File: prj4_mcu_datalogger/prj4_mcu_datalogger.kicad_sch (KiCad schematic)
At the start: 25 parts, among them U1 24LC1025, U2 24LC1025, U3 DS1337S+, U4 ATMEGA328P-AU, Y1 Crystal, Y2 Crystal

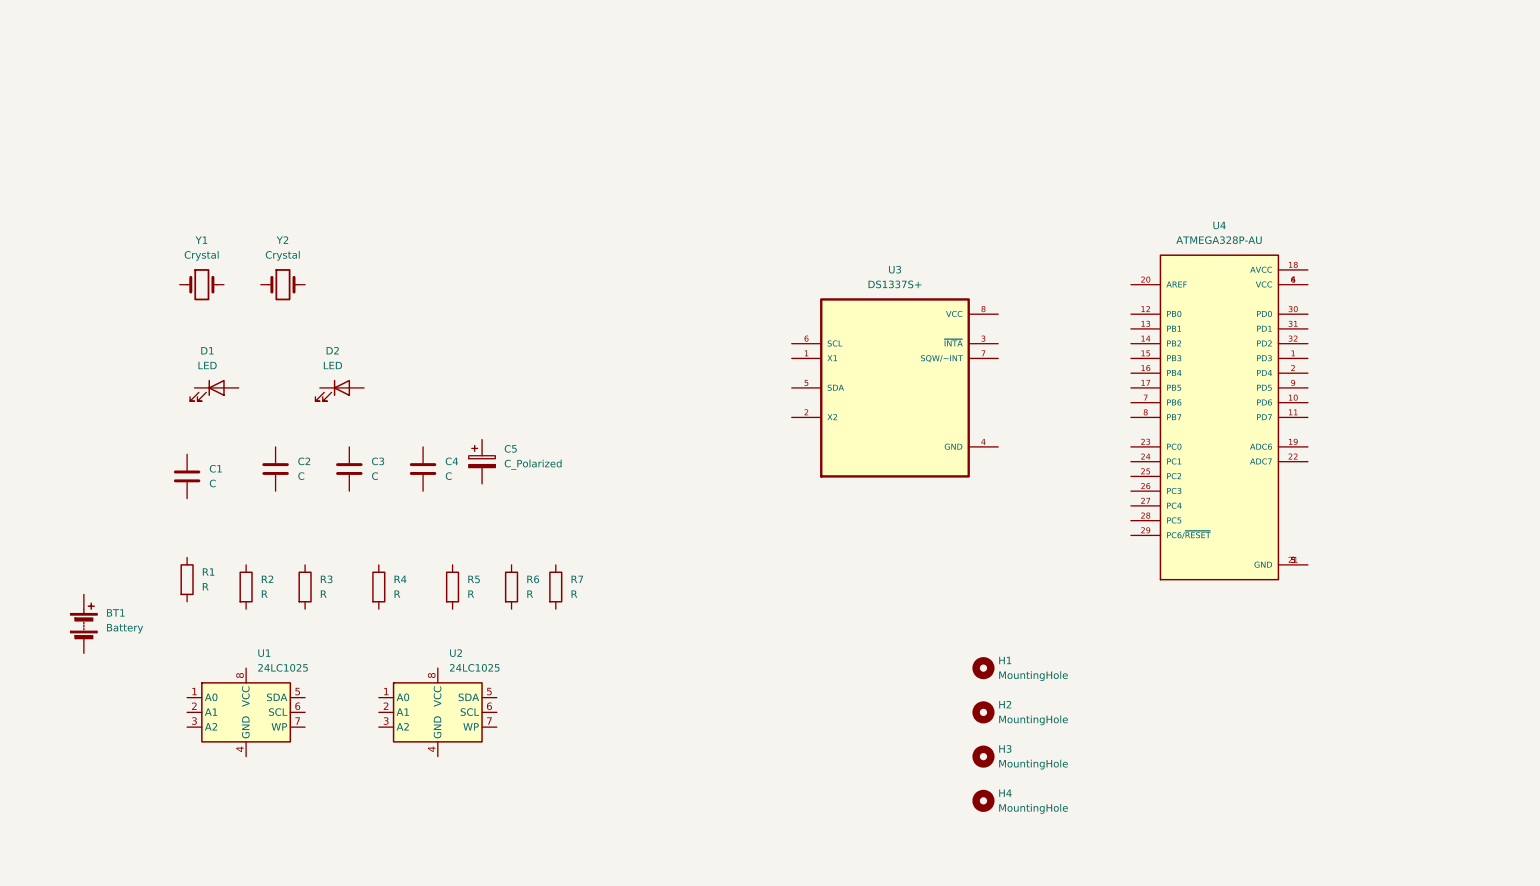
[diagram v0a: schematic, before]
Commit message: Nuovo foglio e posizionamento componenti
Feat: creato sheet "Connectors"
Feat: posizionati i componenti
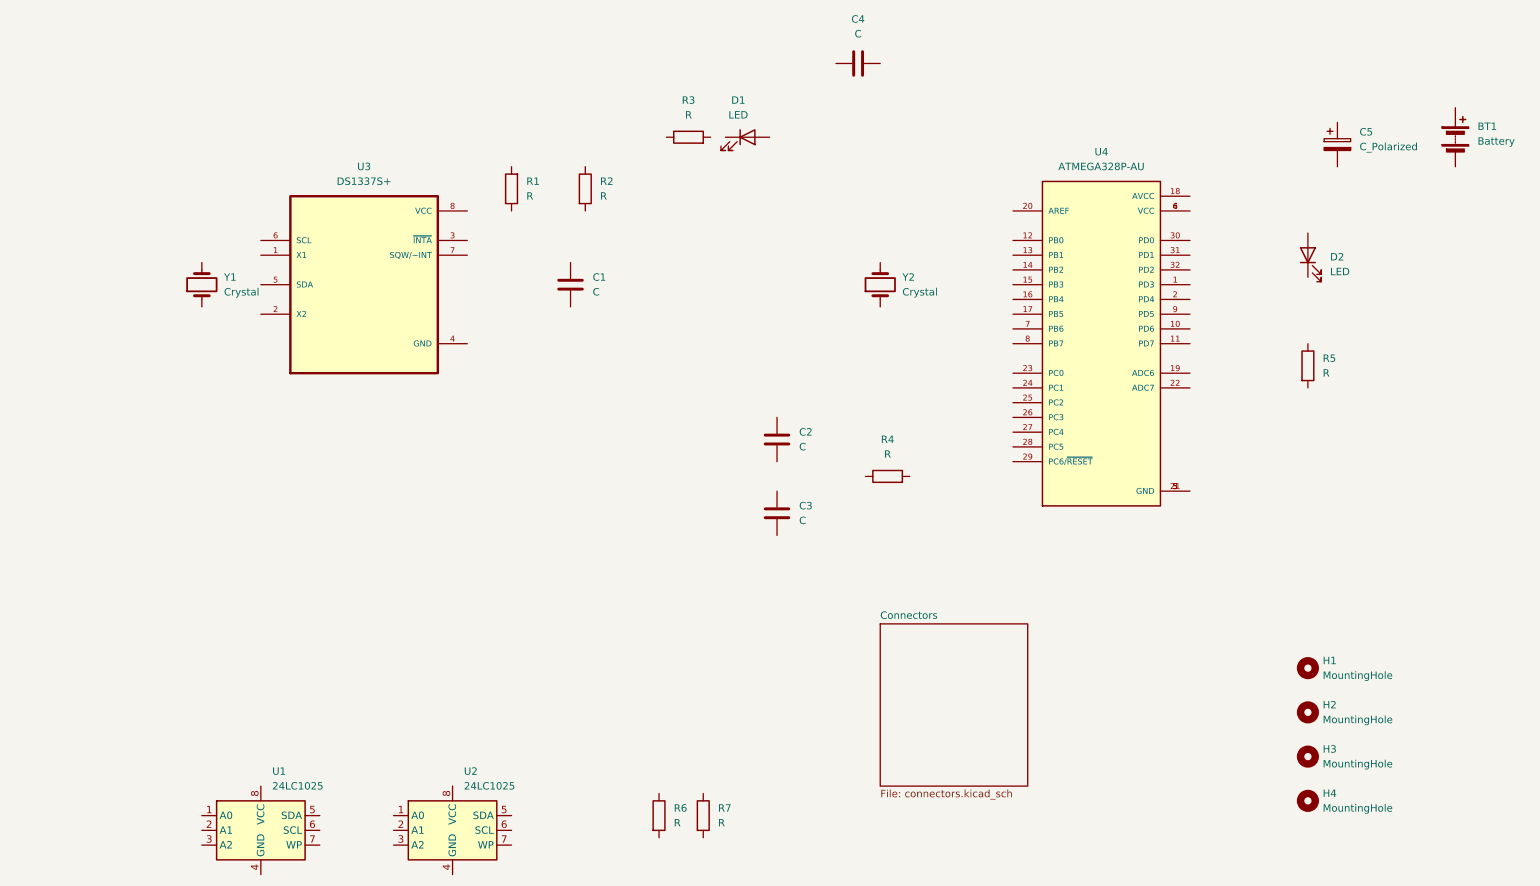
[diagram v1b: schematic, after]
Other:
- added sheet Connectors (connectors.kicad_sch)
- moved on the sheet: BT1, C1, C2, C3, C4, C5, D1, D2, H1, H2, H3, H4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

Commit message: Associazione simboli/footprint
Feat: associati i simboli dei componenti con i relativi footprint
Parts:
- BT1: footprint (none) -> Connector_PinHeader_2.54mm:PinHeader_1x02_P2.54mm_Vertical
- C1, C4: value C -> 0.1uF; footprint (none) -> Capacitor_SMD:C_0805_2012Metric
- C2, C3: value C -> 22pF; footprint (none) -> Capacitor_SMD:C_0805_2012Metric
- C5: value C_Polarized -> 100nF; footprint (none) -> Capacitor_SMD:C_0805_2012Metric
- D1, D2: footprint (none) -> LED_SMD:LED_0805_2012Metric
- H1, H2, H3, H4: footprint (none) -> MountingHole:MountingHole_2.1mm
- R1, R2, R4: value R -> 10K; footprint (none) -> Resistor_SMD:R_0805_2012Metric
- R3, R5: value R -> 330; footprint (none) -> Resistor_SMD:R_0805_2012Metric
- R6, R7: value R -> 4.7K; footprint (none) -> Resistor_SMD:R_0805_2012Metric
- U1, U2: footprint (none) -> Package_SO:SOIC-8_5.23x5.23mm_P1.27mm
- U3: footprint SOIC127P600X175-8N -> DS1337S:SOIC127P600X175-8N
- U4: footprint QFP80P900X900X120-32N -> ATMEGA328P-AU:QFP80P900X900X120-32N
- Y1: value Crystal -> 32.768 KHz; footprint (none) -> Crystal:Crystal_SMD_5032-2Pin_5.0x3.2mm_HandSoldering
- Y2: value Crystal -> 16 MHz; footprint (none) -> Crystal:Crystal_SMD_5032-2Pin_5.0x3.2mm_HandSoldering
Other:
- moved on the sheet: C1, R1, R2

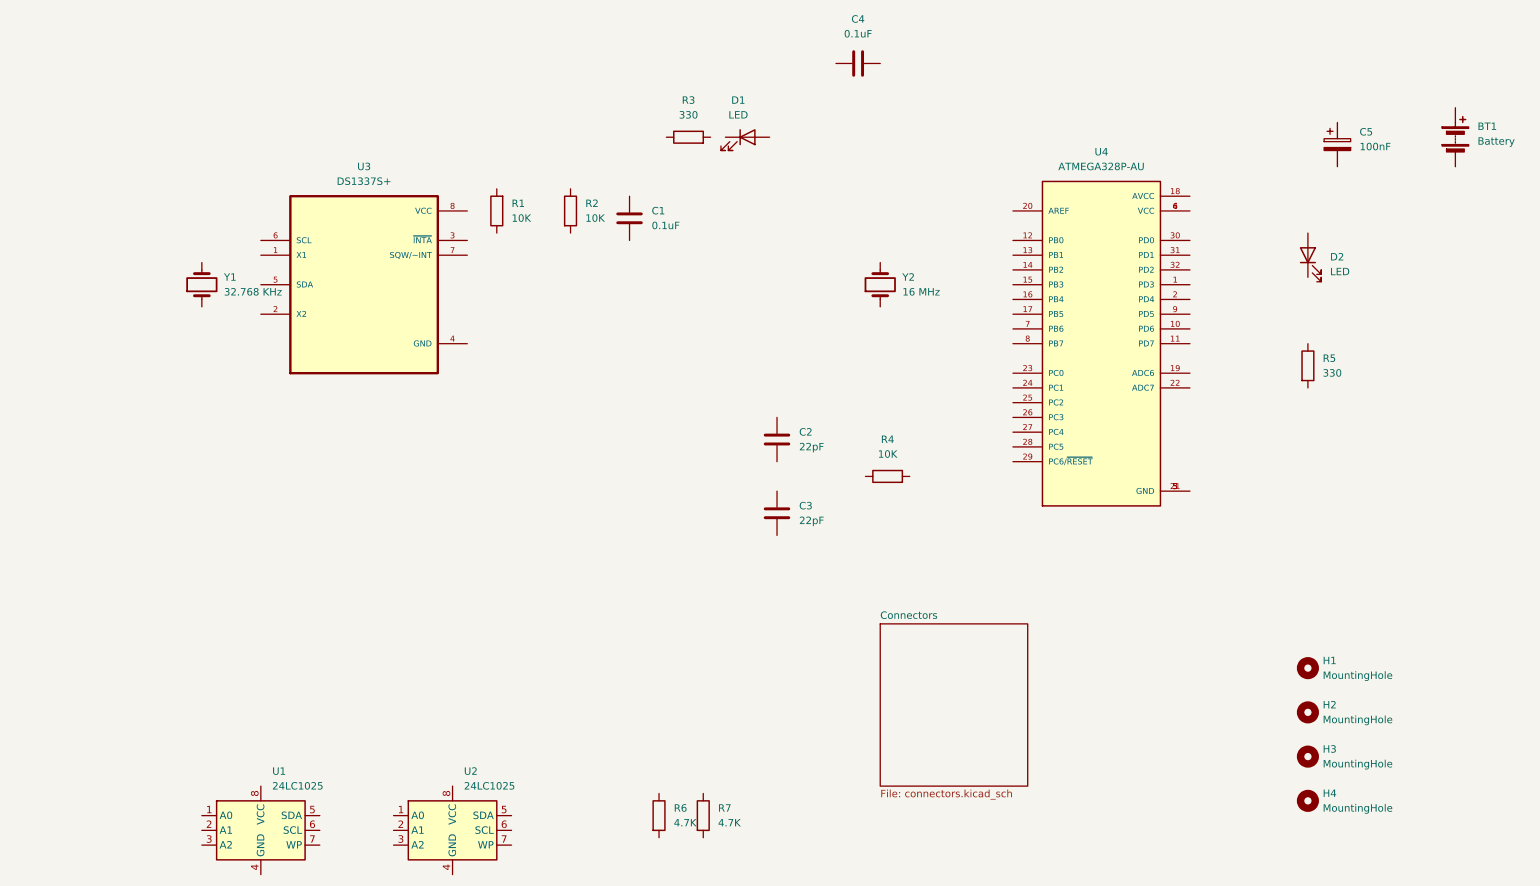
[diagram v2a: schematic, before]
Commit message: Completate le connessioni nello schematico
Feat: connessi tutti i pin in entrambi i fogli
Feat: effettuato ERC
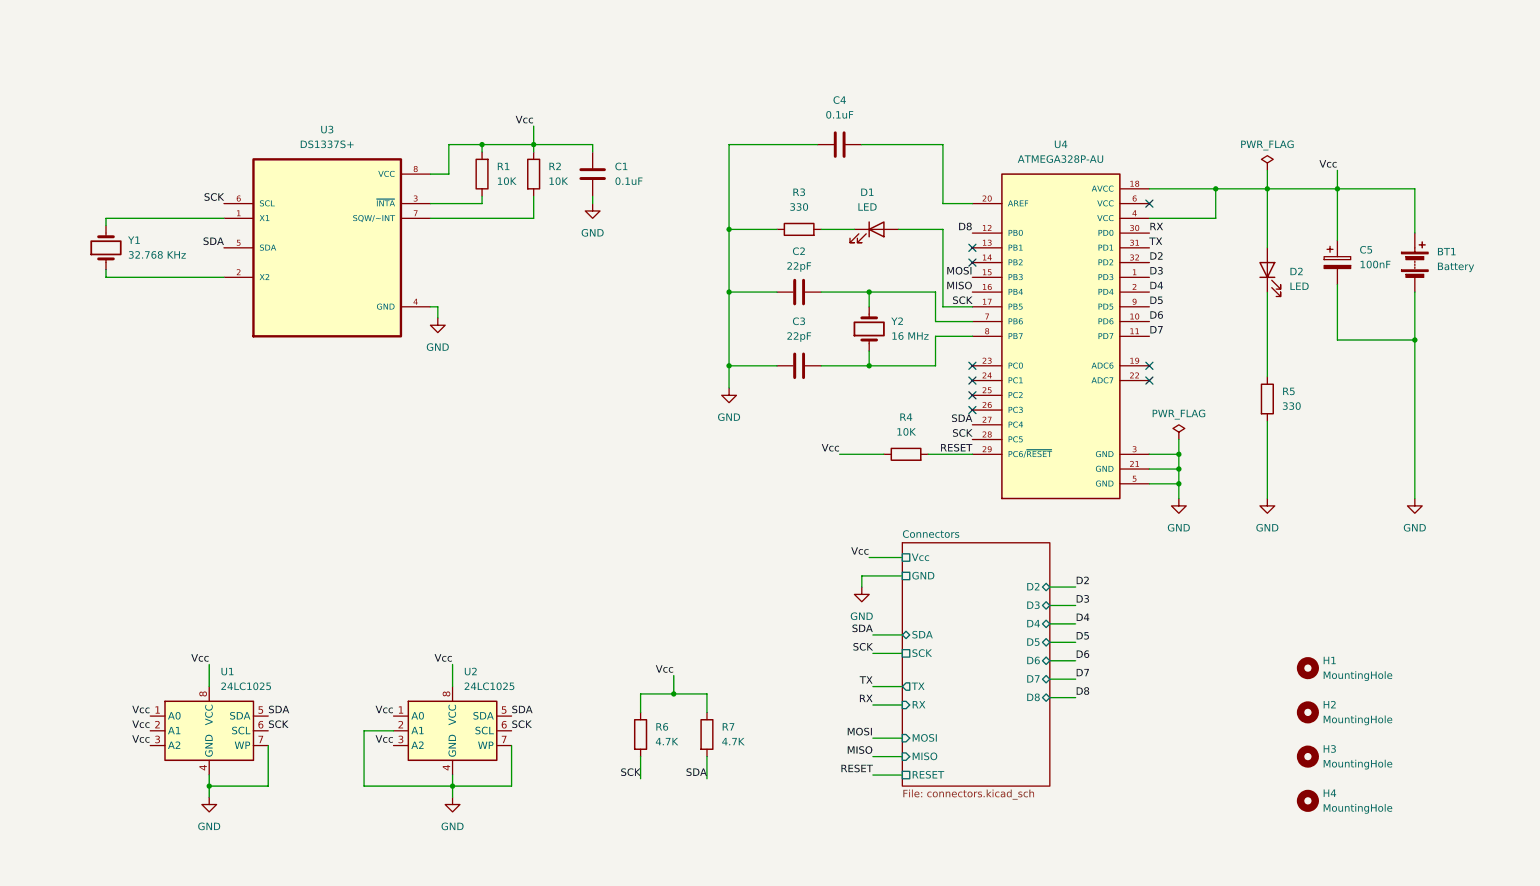
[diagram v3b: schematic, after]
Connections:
- net at U3.1 (X1): now also Y1.2
- net at U3.2 (X2): now also Y1.1
- net at U3.3 (~{INTA}): now also R1.1
- net GND: now reaches U3.4 (GND)
- net GND: now also BT1.2 (-), C1.2, C2.1, C3.1, C4.1, C5.2, R3.1, R5.2, U1.4 (GND), U1.7 (WP), U2.2 (A1), U2.4 (GND), U2.7 (WP), U4.21 (GND), U4.3 (GND), U4.5 (GND)
- net SDA: now reaches U3.5 (SDA)
- net SDA: now also R7.2, U1.5 (SDA), U2.5 (SDA), U4.27 (PC4)
- net SCK: now reaches U3.6 (SCL)
- net SCK: now also D1.2 (A), R6.2, U1.6 (SCL), U2.6 (SCL), U4.17 (PB5), U4.28 (PC5)
- net at U3.7 (SQW/~INT): now also R2.2
- net Vcc: now reaches U3.8 (VCC)
- net Vcc: now also BT1.1 (+), C1.1, C5.1, D2.2 (A), R1.2, R2.1, R4.1, R6.1, R7.1, U1.1 (A0), U1.2 (A1), U1.3 (A2), U1.8 (VCC), U2.1 (A0), U2.3 (A2), U2.8 (VCC), U4.18 (AVCC), U4.4 (VCC)
- net at R3.2: now also D1.1 (K)
- net D3: now reaches U4.1 (PD3)
- net D6: now reaches U4.10 (PD6)
- net D7: now reaches U4.11 (PD7)
- net D8: now reaches U4.12 (PB0)
- net MOSI: now reaches U4.15 (PB3)
- net MISO: now reaches U4.16 (PB4)
- net D4: now reaches U4.2 (PD4)
- net at U4.20 (AREF): now also C4.2
- net RESET: now reaches U4.29 (PC6/~{RESET})
- net RESET: now also R4.2
- net RX: now reaches U4.30 (PD0)
- net TX: now reaches U4.31 (PD1)
- net D2: now reaches U4.32 (PD2)
- net at U4.6 (VCC): no longer U4.4 (VCC)
- net at U4.7 (PB6): now also C2.2, Y2.2
- net at U4.8 (PB7): now also C3.2, Y2.1
- net D5: now reaches U4.9 (PD5)
- net at R5.1: now also D2.1 (K)
- no-connect marks 0 -> 9
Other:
- sheet Connectors ports: added D2, D3, D4, D5, D6, D7, D8, GND, MISO, MOSI, RESET, RX, SCK, SDA, TX, Vcc; removed none
- moved on the sheet: BT1, C1, C2, C3, C4, C5, D1, D2, R1, R2, R3, R4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

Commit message: Inseriti commenti nello schema
Feat: aggiunti commenti nello schema elettrico
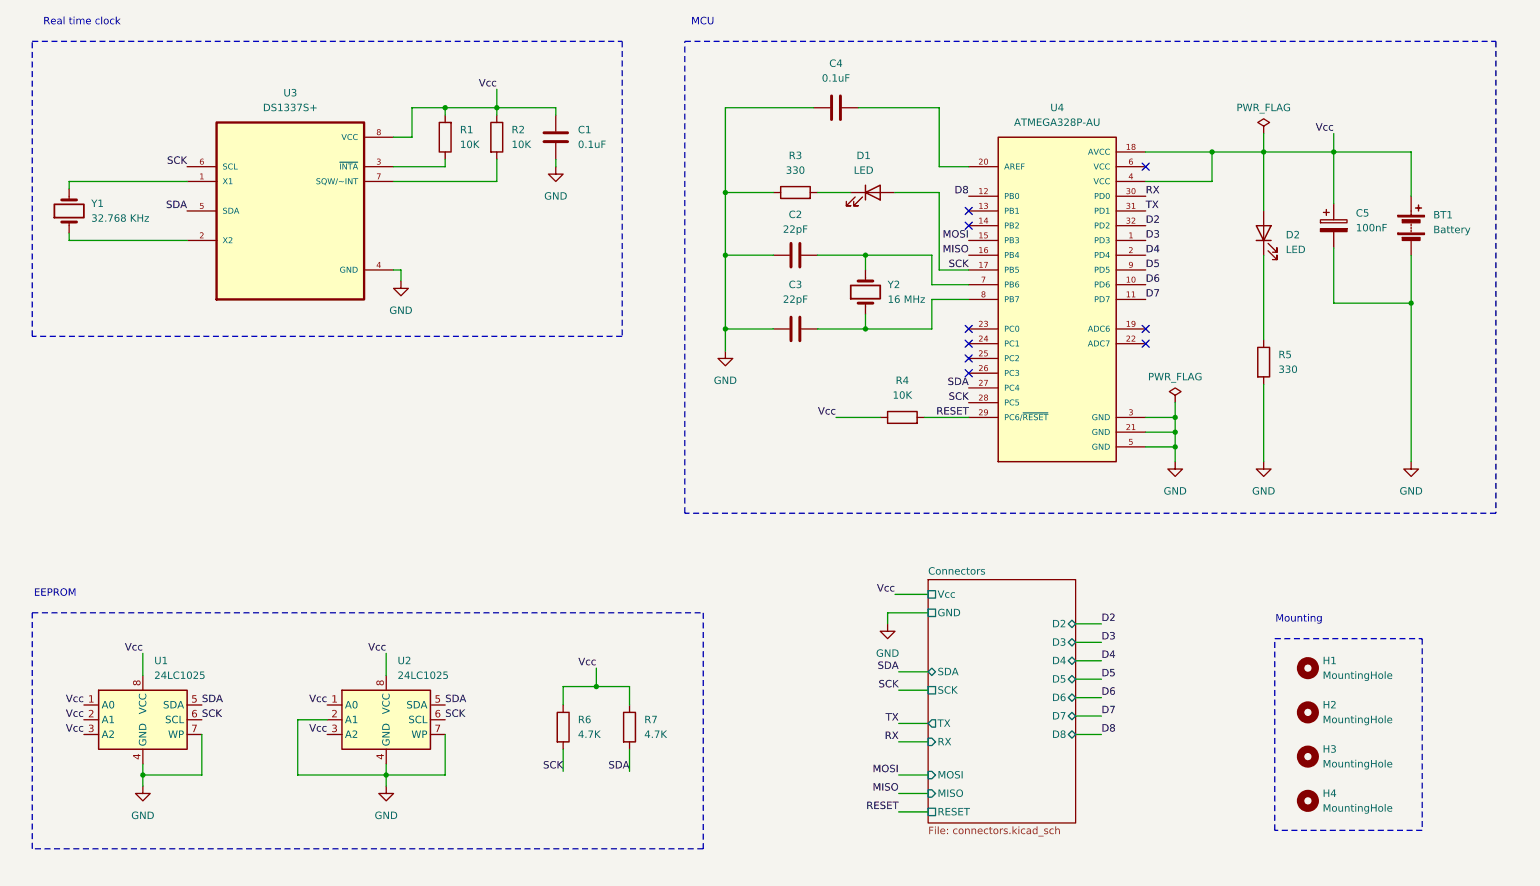
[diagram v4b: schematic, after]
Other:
- note added: "EEPROM"
- note added: "MCU"
- note added: "Mounting"
- note added: "Real time clock"
- moved on the sheet: BT1, C1, C2, C3, C4, C5, D1, D2, R1, R2, R3, R4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

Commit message: Ri-annotati tutti i componenti
Fix: cancellate annotazioni e ricreate con ordinamento per posizione Y
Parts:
- renumbered C4 to C1, C1 to C2, C5 to C3, C2 to C4, C3 to C5, R5 to R4, R4 to R5, U3 to U1, U4 to U2, U1 to U3, U2 to U4

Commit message: Correzione SCK
Fix: SCL era nominato SCK (erano in corto), ora sono separati
Fix: numerati i REF degli elementi grafici su Pcbnew
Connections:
- net SCK: no longer R6.2, U1.6 (SCL), U2.28 (PC5), U3.6 (SCL), U4.6 (SCL)
- new net SCL: R6.2, U1.6 (SCL), U2.28 (PC5), U3.6 (SCL), U4.6 (SCL)
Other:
- sheet Connectors ports: added SCL; removed none
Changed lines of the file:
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@@
     (stroke (width 0) (type default))
   )
-  (wire (pts (xy 173.355 144.145) (xy 178.435 144.145))
+  (wire (pts (xy 173.355 142.24) (xy 178.435 142.24))
     (stroke (width 0) (type default))
   )
@@
     (stroke (width 0) (type default))
   )
+  (wire (pts (xy 173.355 149.86) (xy 178.435 149.86))
+    (stroke (width 0) (type default))
+  )
   (wire (pts (xy 104.14 50.8) (xy 104.14 46.99))
     (stroke (width 0) (type default))
@@
     (stroke (width 0) (type default))
   )
-  (wire (pts (xy 173.355 147.32) (xy 178.435 147.32))
+  (wire (pts (xy 173.355 145.415) (xy 178.435 145.415))
     (stroke (width 0) (type default))
   )
@@
     (effects (font (size 1.27 1.27)) (justify right bottom))
   )
-  (label "SCK" (at 95.25 143.51 0) (fields_autoplaced)
+  (label "SCL" (at 95.25 143.51 0) (fields_autoplaced)
     (effects (font (size 1.27 1.27)) (justify left bottom))
   )
@@
     (effects (font (size 1.27 1.27)) (justify right bottom))
   )
-  (label "SCK" (at 173.355 138.43 180) (fields_autoplaced)
+  (label "SCL" (at 173.355 138.43 180) (fields_autoplaced)
     (effects (font (size 1.27 1.27)) (justify right bottom))
   )
@@
     (effects (font (size 1.27 1.27)) (justify right bottom))
   )
-  (label "SCK" (at 53.34 143.51 0) (fields_autoplaced)
+  (label "SCL" (at 53.34 143.51 0) (fields_autoplaced)
     (effects (font (size 1.27 1.27)) (justify left bottom))
   )
@@
     (effects (font (size 1.27 1.27)) (justify left bottom))
   )
-  (label "SCK" (at 50.8 48.26 180) (fields_autoplaced)
+  (label "SCL" (at 50.8 48.26 180) (fields_autoplaced)
     (effects (font (size 1.27 1.27)) (justify right bottom))
   )
@@
     (effects (font (size 1.27 1.27)) (justify left bottom))
   )
-  (label "RX" (at 173.355 147.32 180) (fields_autoplaced)
+  (label "RX" (at 173.355 145.415 180) (fields_autoplaced)
     (effects (font (size 1.27 1.27)) (justify right bottom))
   )
@@
     (effects (font (size 1.27 1.27)) (justify left bottom))
   )
-  (label "SCK" (at 185.42 88.9 180) (fields_autoplaced)
+  (label "SCK" (at 173.355 149.86 180) (fields_autoplaced)
+    (effects (font (size 1.27 1.27)) (justify right bottom))
+  )
+  (label "SCL" (at 185.42 88.9 180) (fields_autoplaced)
     (effects (font (size 1.27 1.27)) (justify right bottom))
   )
@@
     (effects (font (size 1.27 1.27)) (justify right bottom))
   )
-  (label "SCK" (at 115.57 152.4 180) (fields_autoplaced)
+  (label "SCL" (at 115.57 152.4 180) (fields_autoplaced)
     (effects (font (size 1.27 1.27)) (justify right bottom))
   )
@@
     (effects (font (size 1.27 1.27)) (justify right bottom))
   )
-  (label "TX" (at 173.355 144.145 180) (fields_autoplaced)
+  (label "TX" (at 173.355 142.24 180) (fields_autoplaced)
     (effects (font (size 1.27 1.27)) (justify right bottom))
   )
@@
       (effects (font (size 1.27 1.27)) (justify left))
     )
-    (pin "SCK" passive (at 178.435 138.43 180)
+    (pin "SCL" passive (at 178.435 138.43 180)
       (effects (font (size 1.27 1.27)) (justify left))
     )
@@
       (effects (font (size 1.27 1.27)) (justify right))
     )
-    (pin "TX" output (at 178.435 144.145 180)
-      (effects (font (size 1.27 1.27)) (justify left))
-    )
-    (pin "RX" input (at 178.435 147.32 180)
+    (pin "TX" output (at 178.435 142.24 180)
+      (effects (font (size 1.27 1.27)) (justify left))
+    )
+    (pin "RX" input (at 178.435 145.415 180)
       (effects (font (size 1.27 1.27)) (justify left))
     )
@@
       (effects (font (size 1.27 1.27)) (justify left))
     )
+    (pin "SCK" passive (at 178.435 149.86 180)
+      (effects (font (size 1.27 1.27)) (justify left))
+    )
